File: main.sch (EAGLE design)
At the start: 53 parts, among them X1 ZX62D-B-5PA8

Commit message: Incorporated Feedback
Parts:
- removed U$5: NCV7805, CustomParts:NCV7805
- added C10, C11, C15, C17: 0.1uF, rcl:C-EUC0805
- added C12: 10uF, rcl:C-EUC0805
- added C13: 22uF, rcl:C-EUC0805
- added C14: 100nF, rcl:C-EUC0805
- added C16: 47uF, rcl:C-EUC0805
- added IC1: REG1117, burr-brown:REG1117
- C1: value 0.1uF -> 10uF
- C2: value 0.1uF -> 22uF
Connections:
- net N$1 renamed P+
- net N$2 renamed P-
- removed net N$4: U$5.VIN, U$6.2
- new net 8V4_IN: C10.1, C12.1, IC1.VIN, U$6.2
- net 3V3: now also C15.1
- net GND: now also C10.2, C11.2, C12.2, C13.2, C14.2, C15.2, C16.2, C17.2, IC1.GND, LEFT_A.P, LEFT_B.P, RIGHT_A.P1, RIGHT_B.P1; no longer U$5.GND
- net LEFT_A_SW: now also LEFT_A.S
- net LEFT_B_SW: now also LEFT_B.S
- net RIGHT_A_SW: now also RIGHT_A.S1
- net RIGHT_B_SW: now also RIGHT_B.S1
- net VCC: now also C11.1, C13.1, C14.1, C16.1, C17.1, IC1.VOUT; no longer U$5.VOUT
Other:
- moved on the sheet: 3V_SRC, C1, D1, R18

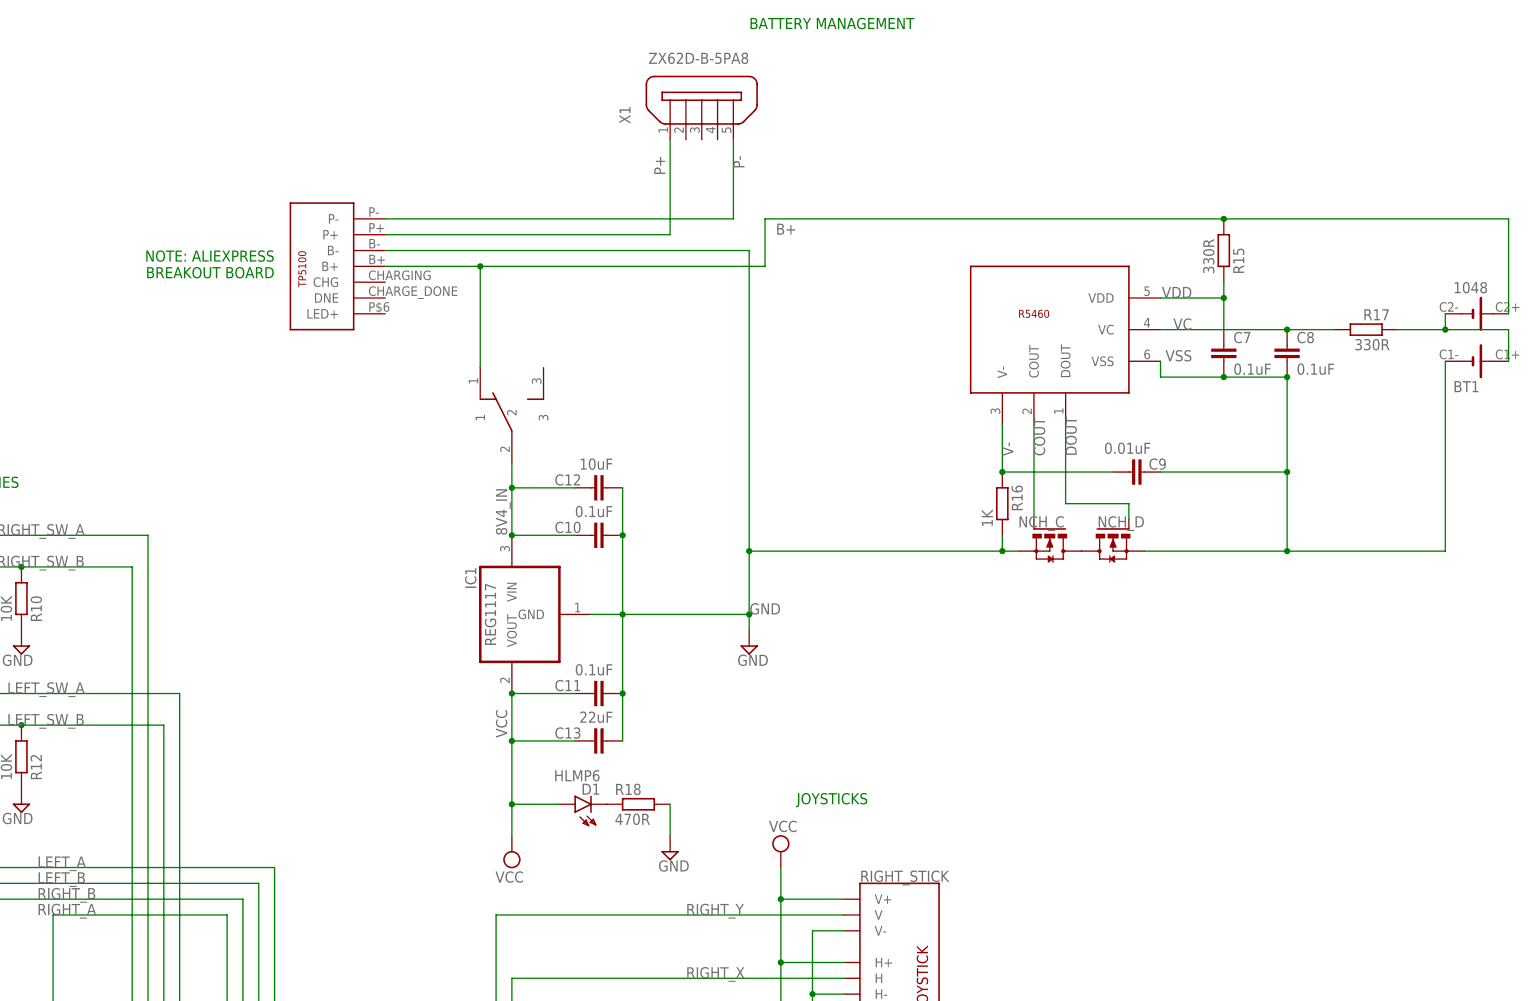
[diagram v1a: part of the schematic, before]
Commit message: Made AA mount
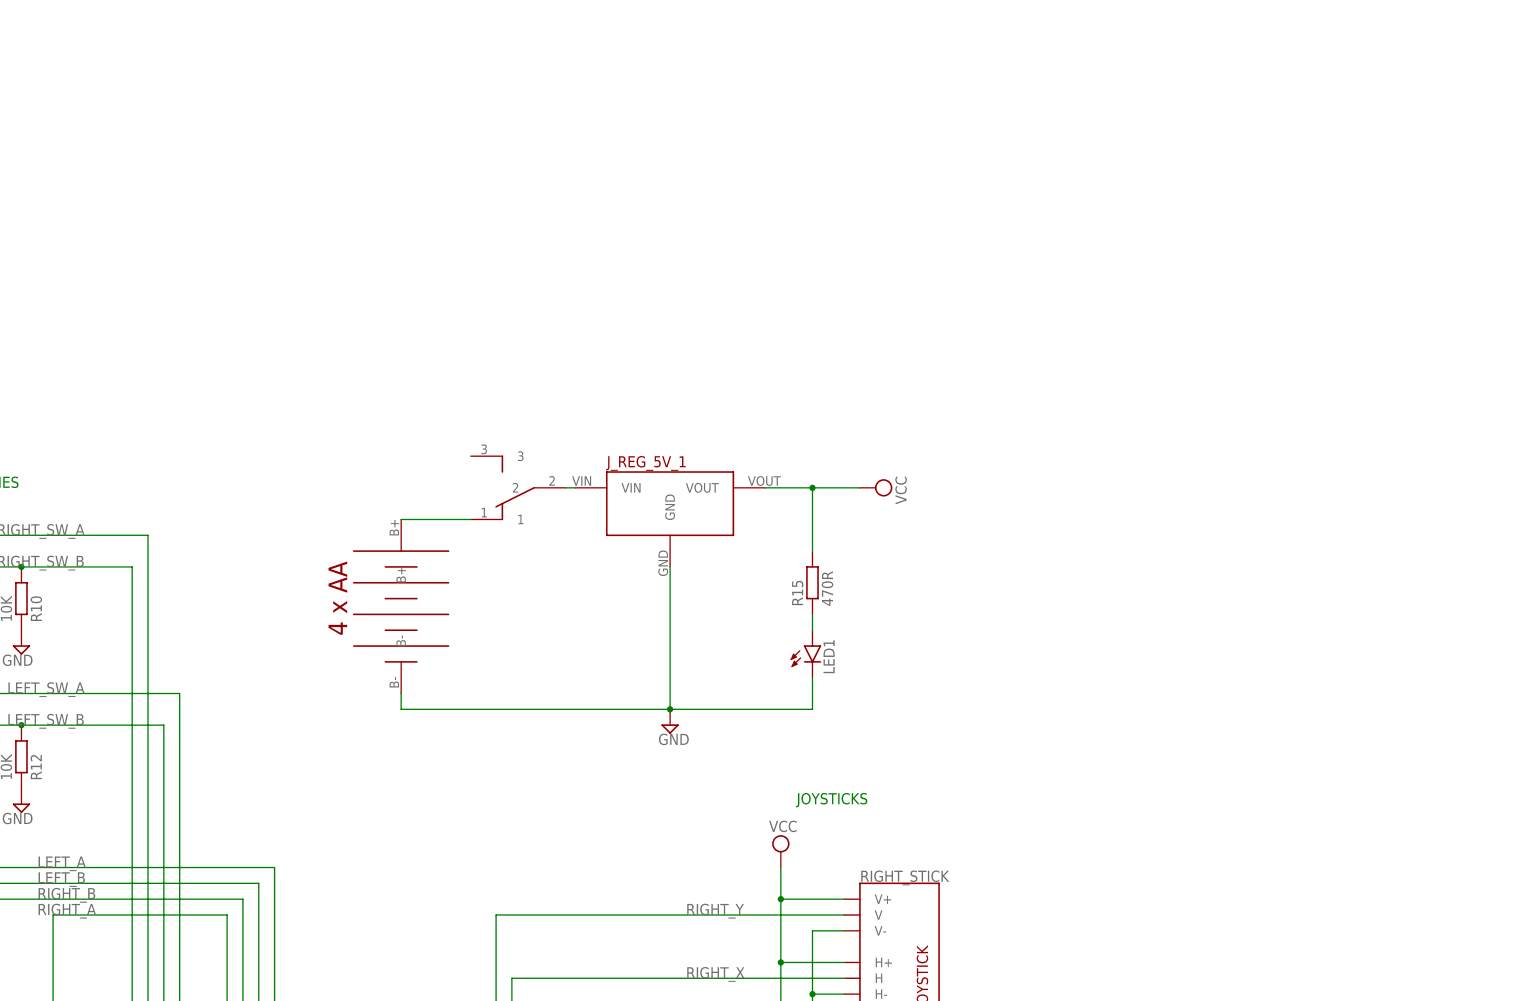
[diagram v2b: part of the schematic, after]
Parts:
- removed BT1: 1048, 1048:1048
- removed C10, C11: 0.1uF, rcl:C-EUC0805
- removed C12: 10uF, rcl:C-EUC0805
- removed C13: 22uF, rcl:C-EUC0805
- removed C7, C8: 0.1uF, SparkFun-Capacitors:0.1UF-0603-25V-(+80/-20%)
- removed C9: 0.01uF, SparkFun-Capacitors:0.1UF-0603-25V-(+80/-20%)
- removed D1: HLMP6, display-hp:HLMP6
- removed IC1: REG1117, burr-brown:REG1117
- removed NCH_C, NCH_D: FQD13N06LTM, Transistor:FQD13N06LTM
- removed R16: 1K, eagle-ltspice:R
- removed R17: 330R, eagle-ltspice:R
- removed R18: 470R, eagle-ltspice:R
- removed R5460: R5460, CustomParts:R5460
- removed U$6: EG1201, CustomParts:EG1201
- removed X1: ZX62D-B-5PA8, zx62d-b-5pa8-oshpark_10:ZX62D-B-5PA8
- added J_REG_5V_1: 5V_VOLTAGE_REGULATOR, Pololu Voltage Regulators:5V_VOLTAGE_REGULATOR
- added LED1: (no value), led:LED5MM
- added U$3: 4XAA, CustomParts:4XAA
- R15: value 330R -> 470R
- U$4: value TP5100_MODULE -> EG1201; device CustomParts:TP5100_MODULE -> CustomParts:EG1201
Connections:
- removed net 8V4_IN: C10.1, C12.1, IC1.VIN, U$6.2
- removed net B+: BT1.C2+, R15.2, U$4.B+, U$6.1
- removed net BM: BT1.C1+, BT1.C2-, R17.1
- removed net COUT: NCH_C.G, R5460.COUT
- removed net DOUT: NCH_D.G, R5460.DOUT
- removed net N$5: D1.K, R18.1
- removed net P+: U$4.P+, X1G$1.1
- removed net P-: U$4.P-, X1G$1.5
- removed net V-: C9.1, R16.2, R5460.V-
- removed net VC: C8.1, R17.2, R5460.VC
- removed net VDD: C7.1, R15.1, R5460.VDD
- removed net VSS: BT1.C1-, C7.2, C8.2, C9.2, NCH_D.S, R5460.VSS
- new net N$1: U$3.B+, U$4.1
- new net N$2: J_REG_5V_1.VIN, U$4.2
- net GND: now also J_REG_5V_1.GND, LED1.C, U$3.B-; no longer C10.2, C11.2, C12.2, C13.2, IC1.GND, NCH_C.S, R16.1, R18.2, U$4.B-
- net N$3: now also LED1.A, R15.1; no longer NCH_C.D, NCH_D.D
- net VCC: now also J_REG_5V_1.VOUT, R15.2; no longer C11.1, C13.1, D1.A, IC1.VOUT
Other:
- note removed: "BATTERY MANAGEMENT"
- note removed: "NOTE: ALIEXPRESS BREAKOUT BOARD"
- moved on the sheet: R15

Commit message: Made silkscreen touches
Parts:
- removed J_REG_5V_1: 5V_VOLTAGE_REGULATOR, Pololu Voltage Regulators:5V_VOLTAGE_REGULATOR
- removed U$3: 4XAA, CustomParts:4XAA
- added SV3: (no value), con-lstb:MA04-1
- added X1: ZX62D-B-5PA8, zx62d-b-5pa8-oshpark_10:ZX62D-B-5PA8
- R15: value 470R -> 470
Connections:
- removed net N$1: U$3.B+, U$4.1
- removed net N$2 (its old number): J_REG_5V_1.VIN, U$4.2
- new net INPUT_V: U$4.3, X1G$1.1
- new net SCL: SV3.2, U$1.3
- new net SDA: SV3.1, U$1.2
- net GND: now also SV3.3, X1G$1.5; no longer J_REG_5V_1.GND, U$3.B-
- net RIGHT_STICK_SW: now also U$1.4; no longer U$1.2
- net RIGHT_SW_A: now also U$1.5; no longer U$1.3
- net RIGHT_SW_B: now also U$1.6; no longer U$1.4
- net VCC: now also SV3.4, U$4.2; no longer J_REG_5V_1.VOUT
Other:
- note added: "I2C HEADER"
- note added: "INPUT 5V"
- note added: "ON LED"
- moved on the sheet: LED1, R15

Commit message: Final version 1 changes
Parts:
- removed C1: 10uF, rcl:C-EUC0805
- added C7: 22µF, AVX_By_element14_Batch_1:TAJA226K010RNJ
- added U1: 0ZCH0075AF2E, CustomParts:0ZCH0075AF2E
- 3V_SRC: value V_REG_LD1117VXXLD1117-SMD -> (none); device CUSTOM-SparkFun-IC-Power:V_REG_LD1117VXXLD1117-SMD -> CUSTOM-SparkFun-IC-Power:V_REG_LM1117SOT223
- C2: value 22uF -> 10µF; device rcl:C-EUC0805 -> AVX_By_element14_Batch_1:TAJC106M020R
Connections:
- removed net INPUT_V: U$4.3, X1G$1.1
- new net FUSE: U1.2, X1G$1.1
- new net N$3: U$4.3, U1.1
- net 3V3: now also C7.C1; no longer C2.1
- net GND: now also 3V_SRC.ADJ, C2.C2, C7.C2; no longer 3V_SRC.GND, C1.2, C2.2
- net VCC: now also C2.C1; no longer C1.1
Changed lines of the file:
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@@
 <part name="LEFT_SW" library="CustomParts" deviceset="2_POLE_SWITCH" device=""/>
 <part name="RIGHT_SW" library="CustomParts" deviceset="2_POLE_SWITCH" device=""/>
-<part name="3V_SRC" library="CUSTOM-SparkFun-IC-Power" deviceset="V_REG_LD1117VXX" device="LD1117-SMD"/>
-<part name="C1" library="rcl" library_urn="urn:adsk.eagle:library:334" deviceset="C-EU" device="C0805" package3d_urn="urn:adsk.eagle:package:23617/2" value="10uF"/>
-<part name="C2" library="rcl" library_urn="urn:adsk.eagle:library:334" deviceset="C-EU" device="C0805" package3d_urn="urn:adsk.eagle:package:23617/2" value="22uF"/>
+<part name="3V_SRC" library="CUSTOM-SparkFun-IC-Power" deviceset="V_REG_LM1117" device="SOT223"/>
 <part name="SUPPLY1" library="supply2" library_urn="urn:adsk.eagle:library:372" deviceset="GND" device=""/>
 <part name="SUPPLY2" library="supply2" library_urn="urn:adsk.eagle:library:372" deviceset="GND" device=""/>
@@
 <part name="SUPPLY20" library="supply2" library_urn="urn:adsk.eagle:library:372" deviceset="GND" device=""/>
 <part name="SUPPLY21" library="supply2" library_urn="urn:adsk.eagle:library:372" deviceset="VCC" device=""/>
+<part name="U1" library="CustomParts" deviceset="0ZCH0075AF2E" device=""/>
+<part name="C7" library="AVX_By_element14_Batch_1" deviceset="TAJA226K010RNJ" device="" value="22µF"/>
+<part name="C2" library="AVX_By_element14_Batch_1" deviceset="TAJC106M020R" device="" value="10µF"/>
 </parts>
 <sheets>
@@
 </instance>
 <instance part="3V_SRC" gate="G$1" x="-5.08" y="-10.16" smashed="yes" rot="R180">
-<attribute name="NAME" x="-7.62" y="-2.54" size="1.778" layer="95" rot="R180"/>
-</instance>
-<instance part="C1" gate="G$1" x="15.24" y="-2.54" smashed="yes" rot="R180">
-<attribute name="NAME" x="13.716" y="-2.921" size="1.778" layer="95" rot="R180"/>
-<attribute name="VALUE" x="13.716" y="2.159" size="1.778" layer="96" rot="R180"/>
-</instance>
-<instance part="C2" gate="G$1" x="-25.4" y="-2.54" smashed="yes" rot="R180">
-<attribute name="NAME" x="-26.924" y="-2.921" size="1.778" layer="95" rot="R180"/>
-<attribute name="VALUE" x="-26.924" y="2.159" size="1.778" layer="96" rot="R180"/>
+<attribute name="NAME" x="-5.08" y="-2.54" size="1.778" layer="95" rot="R180"/>
 </instance>
 <instance part="SUPPLY1" gate="GND" x="-5.08" y="7.62" smashed="yes" rot="R180">
@@
 </instance>
 <instance part="C14" gate="G$1" x="5.08" y="-2.54" smashed="yes" rot="R180">
-<attribute name="NAME" x="3.556" y="-2.921" size="1.778" layer="95" rot="R180"/>
+<attribute name="NAME" x="4.699" y="4.064" size="1.778" layer="95" rot="R90"/>
 <attribute name="VALUE" x="3.556" y="2.159" size="1.778" layer="96" rot="R180"/>
 </instance>
 <instance part="C15" gate="G$1" x="-15.24" y="-2.54" smashed="yes" rot="R180">
-<attribute name="NAME" x="-16.764" y="-2.921" size="1.778" layer="95" rot="R180"/>
+<attribute name="NAME" x="-15.621" y="4.064" size="1.778" layer="95" rot="R90"/>
 <attribute name="VALUE" x="-16.764" y="2.159" size="1.778" layer="96" rot="R180"/>
 </instance>
@@
 <attribute name="VALUE" x="97.536" y="-2.921" size="1.778" layer="96" rot="R180"/>
 </instance>
-<instance part="U$4" gate="A" x="73.66" y="111.76" smashed="yes" rot="R180"/>
+<instance part="U$4" gate="A" x="73.66" y="88.9" smashed="yes" rot="R180"/>
 <instance part="X1" gate="G$1" x="83.82" y="129.54" smashed="yes" rot="R90">
 <attribute name="NAME" x="72.39" y="127" size="1.778" layer="95" font="vector" rot="R90"/>
 <attribute name="VALUE" x="91.44" y="138.43" size="1.778" layer="96" font="vector" rot="R180"/>
 </instance>
-<instance part="SUPPLY16" gate="GND" x="88.9" y="96.52" smashed="yes">
-<attribute name="VALUE" x="86.995" y="93.345" size="1.778" layer="96"/>
-</instance>
-<instance part="SUPPLY17" gate="G$1" x="73.66" y="96.52" smashed="yes" rot="R180">
-<attribute name="VALUE" x="75.565" y="93.345" size="1.778" layer="96" rot="R180"/>
+<instance part="SUPPLY16" gate="GND" x="88.9" y="76.2" smashed="yes">
+<attribute name="VALUE" x="86.995" y="73.025" size="1.778" layer="96"/>
+</instance>
+<instance part="SUPPLY17" gate="G$1" x="73.66" y="78.74" smashed="yes" rot="R180">
+<attribute name="VALUE" x="75.565" y="75.565" size="1.778" layer="96" rot="R180"/>
 </instance>
 <instance part="LED1" gate="G$1" x="114.3" y="114.3" smashed="yes">
@@
 <instance part="SUPPLY21" gate="G$1" x="40.64" y="-66.04" smashed="yes">
 <attribute name="VALUE" x="40.005" y="-62.865" size="1.778" layer="96" rot="R90"/>
+</instance>
+<instance part="U1" gate="A" x="78.74" y="109.22" smashed="yes" rot="R90">
+<attribute name="NAME" x="72.1614" y="101.9556" size="2.0828" layer="95" ratio="6" rot="SR90"/>
+<attribute name="VALUE" x="74.7014" y="101.3206" size="2.0828" layer="96" ratio="6" rot="SR90"/>
+</instance>
+<instance part="C7" gate="A" x="-25.4" y="-5.08" smashed="yes" rot="R90">
+<attribute name="VALUE" x="-26.035" y="2.7432" size="2.0828" layer="96" ratio="10" rot="SR180"/>
+<attribute name="NAME" x="-25.6286" y="4.1656" size="2.0828" layer="95" ratio="10" rot="SR90"/>
+</instance>
+<instance part="C2" gate="A" x="15.24" y="-5.08" smashed="yes" rot="R90">
+<attribute name="VALUE" x="22.225" y="2.7432" size="2.0828" layer="96" ratio="10" rot="SR180"/>
+<attribute name="NAME" x="15.0114" y="4.1656" size="2.0828" layer="95" ratio="10" rot="SR90"/>
 </instance>
 </instances>
@@
 <segment>
 <pinref part="3V_SRC" gate="G$1" pin="OUT"/>
-<pinref part="C2" gate="G$1" pin="1"/>
 <wire x1="-12.7" y1="-10.16" x2="-15.24" y2="-10.16" width="0.1524" layer="91"/>
 <wire x1="-15.24" y1="-10.16" x2="-25.4" y2="-10.16" width="0.1524" layer="91"/>
-<wire x1="-25.4" y1="-10.16" x2="-25.4" y2="-5.08" width="0.1524" layer="91"/>
 <wire x1="-25.4" y1="-10.16" x2="-25.4" y2="-30.48" width="0.1524" layer="91"/>
-<junction x="-25.4" y="-10.16"/>
 <pinref part="U$2" gate="G$1" pin="VDD_3V3"/>
 <wire x1="-38.1" y1="-30.48" x2="-25.4" y2="-30.48" width="0.1524" layer="91"/>
@@
 <junction x="-7.62" y="-30.48"/>
 <label x="-20.32" y="-10.16" size="1.778" layer="95"/>
+<pinref part="C7" gate="A" pin="C1"/>
+<wire x1="-25.4" y1="-5.08" x2="-25.4" y2="-10.16" width="0.1524" layer="91"/>
+<junction x="-25.4" y="-10.16"/>
 <pinref part="C15" gate="G$1" pin="1"/>
 <wire x1="-15.24" y1="-5.08" x2="-15.24" y2="-10.16" width="0.1524" layer="91"/>
@@
 <net name="GND" class="0">
 <segment>
-<pinref part="C1" gate="G$1" pin="2"/>
-<pinref part="C2" gate="G$1" pin="2"/>
 <wire x1="15.24" y1="2.54" x2="5.08" y2="2.54" width="0.1524" layer="91"/>
 <wire x1="5.08" y1="2.54" x2="-5.08" y2="2.54" width="0.1524" layer="91"/>
 <wire x1="-5.08" y1="2.54" x2="-15.24" y2="2.54" width="0.1524" layer="91"/>
-<pinref part="3V_SRC" gate="G$1" pin="GND"/>
+<pinref part="3V_SRC" gate="G$1" pin="ADJ"/>
 <wire x1="-15.24" y1="2.54" x2="-25.4" y2="2.54" width="0.1524" layer="91"/>
 <wire x1="-5.08" y1="-2.54" x2="-5.08" y2="2.54" width="0.1524" layer="91"/>
@@
 <pinref part="C15" gate="G$1" pin="2"/>
 <junction x="-15.24" y="2.54"/>
+<pinref part="C7" gate="A" pin="C2"/>
+<pinref part="C2" gate="A" pin="C2"/>
 </segment>
 <segment>
@@
 </segment>
 <segment>
-<pinref part="X1" gate="G$1" pin="5"/>
-<wire x1="88.9" y1="124.46" x2="88.9" y2="99.06" width="0.1524" layer="91"/>
-<pinref part="SUPPLY16" gate="GND" pin="GND"/>
-</segment>
-<segment>
 <pinref part="LED1" gate="G$1" pin="C"/>
 <pinref part="SUPPLY18" gate="GND" pin="GND"/>
@@
 <pinref part="SV3" gate="1" pin="3"/>
 <pinref part="SUPPLY20" gate="GND" pin="GND"/>
+</segment>
+<segment>
+<pinref part="X1" gate="G$1" pin="5"/>
+<pinref part="SUPPLY16" gate="GND" pin="GND"/>
+<wire x1="88.9" y1="124.46" x2="88.9" y2="78.74" width="0.1524" layer="91"/>
 </segment>
 </net>
@@
 <net name="VCC" class="0">
 <segment>
-<pinref part="C1" gate="G$1" pin="1"/>
-<wire x1="15.24" y1="-5.08" x2="15.24" y2="-10.16" width="0.1524" layer="91"/>
 <pinref part="3V_SRC" gate="G$1" pin="IN"/>
-<wire x1="15.24" y1="-10.16" x2="5.08" y2="-10.16" width="0.1524" layer="91"/>
 <wire x1="5.08" y1="-10.16" x2="2.54" y2="-10.16" width="0.1524" layer="91"/>
-<wire x1="15.24" y1="-10.16" x2="25.4" y2="-10.16" width="0.1524" layer="91"/>
-<junction x="15.24" y="-10.16"/>
+<wire x1="5.08" y1="-10.16" x2="15.24" y2="-10.16" width="0.1524" layer="91"/>
 <pinref part="SUPPLY6" gate="G$1" pin="VCC"/>
 <pinref part="C14" gate="G$1" pin="1"/>
+<wire x1="15.24" y1="-10.16" x2="25.4" y2="-10.16" width="0.1524" layer="91"/>
 <wire x1="5.08" y1="-5.08" x2="5.08" y2="-10.16" width="0.1524" layer="91"/>
 <junction x="5.08" y="-10.16"/>
+<pinref part="C2" gate="A" pin="C1"/>
+<wire x1="15.24" y1="-5.08" x2="15.24" y2="-10.16" width="0.1524" layer="91"/>
+<junction x="15.24" y="-10.16"/>
 </segment>
 <segment>
@@
 <segment>
 <pinref part="U$4" gate="A" pin="2"/>
-<wire x1="73.66" y1="103.124" x2="73.66" y2="99.06" width="0.1524" layer="91"/>
+<wire x1="73.66" y1="80.264" x2="73.66" y2="81.28" width="0.1524" layer="91"/>
 <pinref part="SUPPLY17" gate="G$1" pin="VCC"/>
 </segment>
@@
 <pinref part="SV3" gate="1" pin="4"/>
 <pinref part="SUPPLY21" gate="G$1" pin="VCC"/>
-</segment>
-</net>
-<net name="INPUT_V" class="0">
-<segment>
-<pinref part="X1" gate="G$1" pin="1"/>
-<pinref part="U$4" gate="A" pin="3"/>
-<wire x1="78.74" y1="124.46" x2="78.74" y2="118.364" width="0.1524" layer="91"/>
 </segment>
 </net>
@@
 </segment>
 </net>
+<net name="FUSE" class="0">
+<segment>
+<pinref part="X1" gate="G$1" pin="1"/>
+<pinref part="U1" gate="A" pin="2"/>
+<wire x1="78.74" y1="121.92" x2="78.74" y2="124.46" width="0.1524" layer="91"/>
+<label x="81.28" y="116.84" size="1.778" layer="95" rot="R90"/>
+</segment>
+</net>
+<net name="N$3" class="0">
+<segment>
+<pinref part="U1" gate="A" pin="1"/>
+<pinref part="U$4" gate="A" pin="3"/>
+<wire x1="78.74" y1="96.52" x2="78.74" y2="95.504" width="0.1524" layer="91"/>
+</segment>
+</net>
